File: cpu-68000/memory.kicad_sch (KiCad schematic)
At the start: 0 parts

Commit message: added memory, peripherals
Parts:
- added C? (x6): 100nF, symbol Device:C_Small
- added C? (x4): 4.7µF, symbol Device:C_Small
- added C?: 22µF, symbol Device:C_Polarized_Small
- added U? (x2): IS61C5128AL-10TLI, Package_SO:TSOP-II-44_10.16x18.41mm_P0.8mm, symbol 68komputer-common:IS61C5128AL-10TLI
- added U? (x2): SST39SF040, Package_LCC:PLCC-32_THT-Socket, symbol 68komputer-common:SST39SF040
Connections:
- new net +5V: C?.1, C?.1, C?.1, C?.1, C?.1, C?.1, C?.1, C?.1, C?.1, C?.1, C?.1, U?.11 (VDD), U?.11 (VDD), U?.32 (VCC), U?.32 (VCC), U?.33 (VDD), U?.33 (VDD)
- new net A1: U?.12 (A0), U?.12 (A0), U?.3 (A0), U?.3 (A0)
- new net A10: U?.20 (A9), U?.20 (A9), U?.26 (A9), U?.26 (A9)
- new net A11: U?.23 (A10), U?.23 (A10), U?.26 (A10), U?.26 (A10)
- new net A12: U?.25 (A11), U?.25 (A11), U?.27 (A11), U?.27 (A11)
- new net A13: U?.28 (A12), U?.28 (A12), U?.4 (A12), U?.4 (A12)
- new net A14: U?.28 (A13), U?.28 (A13), U?.29 (A13), U?.29 (A13)
- new net A15: U?.29 (A14), U?.29 (A14), U?.30 (A14), U?.30 (A14)
- new net A16: U?.3 (A15), U?.3 (A15), U?.38 (A15), U?.38 (A15)
- new net A17: U?.2 (A16), U?.2 (A16), U?.39 (A16), U?.39 (A16)
- new net A18: U?.30 (A17), U?.30 (A17), U?.40 (A17), U?.40 (A17)
- new net A19: U?.1 (A18), U?.1 (A18), U?.41 (A18), U?.41 (A18)
- new net A2: U?.11 (A1), U?.11 (A1), U?.4 (A1), U?.4 (A1)
- new net A3: U?.10 (A2), U?.10 (A2), U?.5 (A2), U?.5 (A2)
- new net A4: U?.6 (A3), U?.6 (A3), U?.9 (A3), U?.9 (A3)
- new net A5: U?.7 (A4), U?.7 (A4), U?.8 (A4), U?.8 (A4)
- new net A6: U?.16 (A5), U?.16 (A5), U?.7 (A5), U?.7 (A5)
- new net A7: U?.17 (A6), U?.17 (A6), U?.6 (A6), U?.6 (A6)
- new net A8: U?.18 (A7), U?.18 (A7), U?.5 (A7), U?.5 (A7)
- new net A9: U?.19 (A8), U?.19 (A8), U?.27 (A8), U?.27 (A8)
- new net D0: U?.13 (D0), U?.9 (I/O0)
- new net D1: U?.10 (I/O1), U?.14 (D1)
- new net D10: U?.13 (I/O2), U?.15 (D2)
- new net D11: U?.14 (I/O3), U?.17 (D3)
- new net D12: U?.18 (D4), U?.31 (I/O4)
- new net D13: U?.19 (D5), U?.32 (I/O5)
- new net D14: U?.20 (D6), U?.35 (I/O6)
- new net D15: U?.21 (D7), U?.36 (I/O7)
- new net D2: U?.13 (I/O2), U?.15 (D2)
- new net D3: U?.14 (I/O3), U?.17 (D3)
- new net D4: U?.18 (D4), U?.31 (I/O4)
- new net D5: U?.19 (D5), U?.32 (I/O5)
- new net D6: U?.20 (D6), U?.35 (I/O6)
- new net D7: U?.21 (D7), U?.36 (I/O7)
- new net D8: U?.13 (D0), U?.9 (I/O0)
- new net D9: U?.10 (I/O1), U?.14 (D1)
- new net GND: C?.2, C?.2, C?.2, C?.2, C?.2, C?.2, C?.2, C?.2, C?.2, C?.2, C?.2, U?.12 (GND), U?.12 (GND), U?.16 (GND), U?.16 (GND), U?.34 (GND), U?.34 (GND)
- new net ~{LDS}: U?.15 (~{WE}), U?.24 (~{OE})
- new net ~{LWE}: U?.31 (~{WE}), U?.37 (~{OE})
- new net ~{RAM_CS}: U?.8 (~{CE}), U?.8 (~{CE})
- new net ~{ROM_CS}: U?.22 (~{CS}), U?.22 (~{CS})
- new net ~{UDS}: U?.15 (~{WE}), U?.24 (~{OE})
- new net ~{UWE}: U?.31 (~{WE}), U?.37 (~{OE})
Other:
- note added: "High"
- note added: "Low"

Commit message: Peripherals and general connection stuff
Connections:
- net ~{LDS} is gone; now on net ~{LWE}: U?.15 (~{WE}), U?.24 (~{OE})
- net ~{UDS} is gone; now on net ~{UWE}: U?.15 (~{WE}), U?.24 (~{OE})
- net ~{LWE}: no longer U?.31 (~{WE}), U?.37 (~{OE})
- net ~{UWE}: no longer U?.31 (~{WE}), U?.37 (~{OE})
- new net ~{LOE}: U?.31 (~{WE}), U?.37 (~{OE})
- new net ~{UOE}: U?.31 (~{WE}), U?.37 (~{OE})
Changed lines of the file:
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@@
     (effects (font (size 1.27 1.27)) (justify right))
   )
-  (hierarchical_label "~{LWE}" (shape input) (at 46.99 86.36 180)
+  (hierarchical_label "~{LOE}" (shape input) (at 46.99 86.36 180)
     (effects (font (size 1.27 1.27)) (justify right))
   )
-  (hierarchical_label "~{LDS}" (shape input) (at 46.99 88.9 180)
+  (hierarchical_label "~{LWE}" (shape input) (at 46.99 88.9 180)
     (effects (font (size 1.27 1.27)) (justify right))
   )
@@
     (effects (font (size 1.27 1.27)) (justify right))
   )
-  (hierarchical_label "~{UWE}" (shape input) (at 46.99 178.435 180)
+  (hierarchical_label "~{UOE}" (shape input) (at 46.99 178.435 180)
     (effects (font (size 1.27 1.27)) (justify right))
   )
-  (hierarchical_label "~{UDS}" (shape input) (at 46.99 180.975 180)
+  (hierarchical_label "~{UWE}" (shape input) (at 46.99 180.975 180)
     (effects (font (size 1.27 1.27)) (justify right))
   )
@@
     (effects (font (size 1.27 1.27)) (justify right))
   )
-  (hierarchical_label "~{LWE}" (shape input) (at 118.11 83.82 180)
+  (hierarchical_label "~{LOE}" (shape input) (at 118.11 83.82 180)
     (effects (font (size 1.27 1.27)) (justify right))
   )
-  (hierarchical_label "~{LDS}" (shape input) (at 118.11 86.36 180)
+  (hierarchical_label "~{LWE}" (shape input) (at 118.11 86.36 180)
     (effects (font (size 1.27 1.27)) (justify right))
   )
@@
     (effects (font (size 1.27 1.27)) (justify right))
   )
-  (hierarchical_label "~{UWE}" (shape input) (at 118.11 175.895 180)
+  (hierarchical_label "~{UOE}" (shape input) (at 118.11 175.895 180)
     (effects (font (size 1.27 1.27)) (justify right))
   )
-  (hierarchical_label "~{UDS}" (shape input) (at 118.11 178.435 180)
+  (hierarchical_label "~{UWE}" (shape input) (at 118.11 178.435 180)
     (effects (font (size 1.27 1.27)) (justify right))
   )

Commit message: More backplane stuff; added footprints for most
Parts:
- removed C?: 22µF, symbol Device:C_Polarized_Small
- added C411, C412: 10µF, Capacitor_Tantalum_SMD:CP_EIA-3216-18_Kemet-A, symbol Device:C_Polarized_Small
- C401, C402, C403, C404, C405, C406, C407, C408, C409, C410: renamed from C?; footprint (none) -> Capacitor_SMD:C_0805_2012Metric
- gave numbers to parts that had none: 4
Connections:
- net +5V: now also C411.1, C412.1
- net GND: now also C411.2, C412.2
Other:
- moved on the sheet: C405, C406, C407, C408, C409, C410

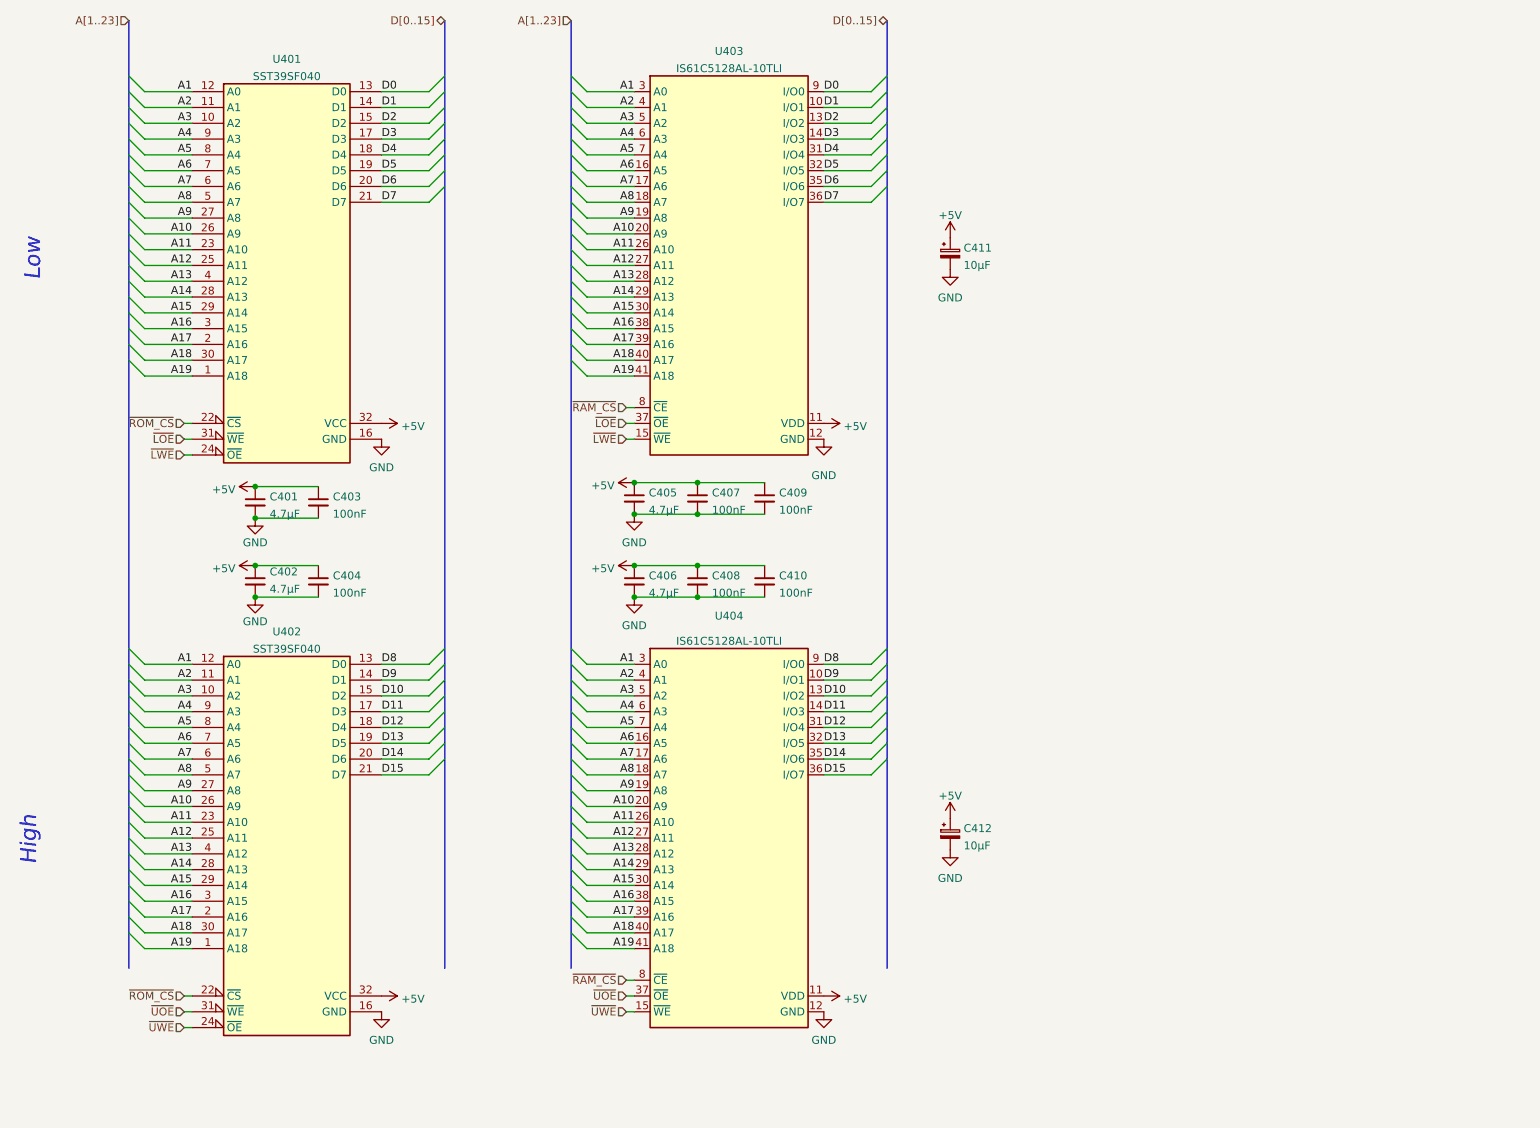
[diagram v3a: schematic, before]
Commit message: start pcb for main cpu
- mostly finish schematic for 68000 cpu; added the missing reset/NMI
  switches

- added footprints for LED indicators

- also added 3d models for fuses, DIN connector, etc
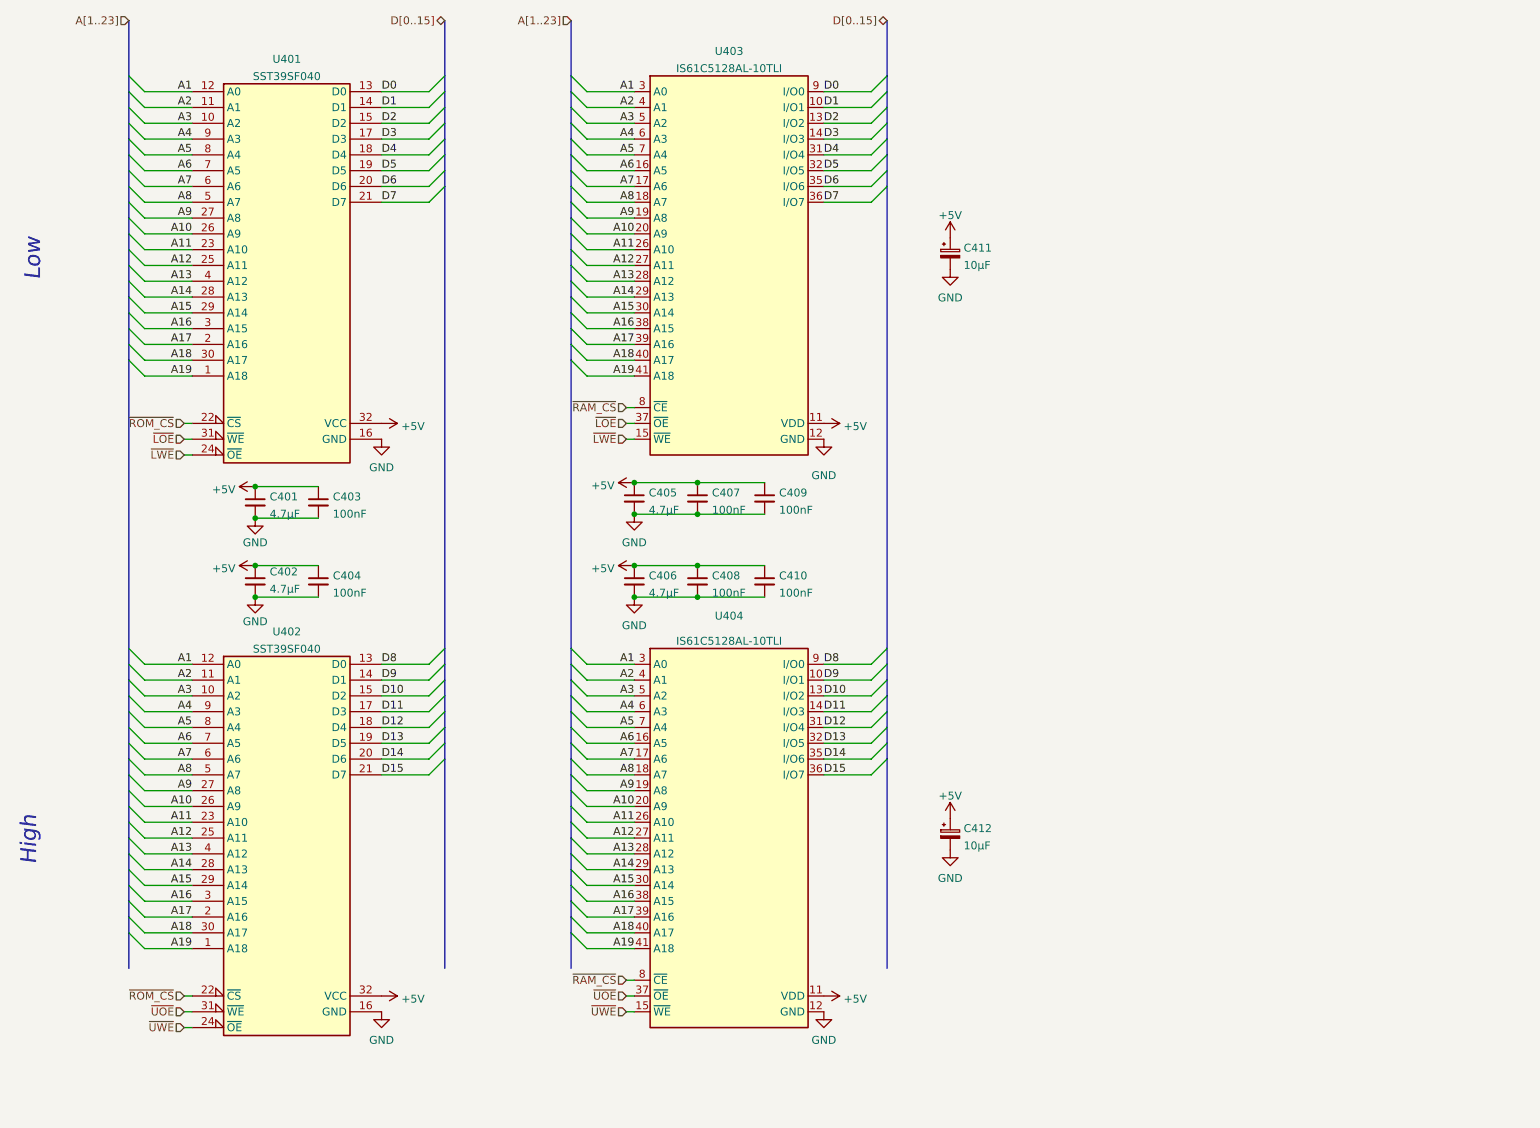
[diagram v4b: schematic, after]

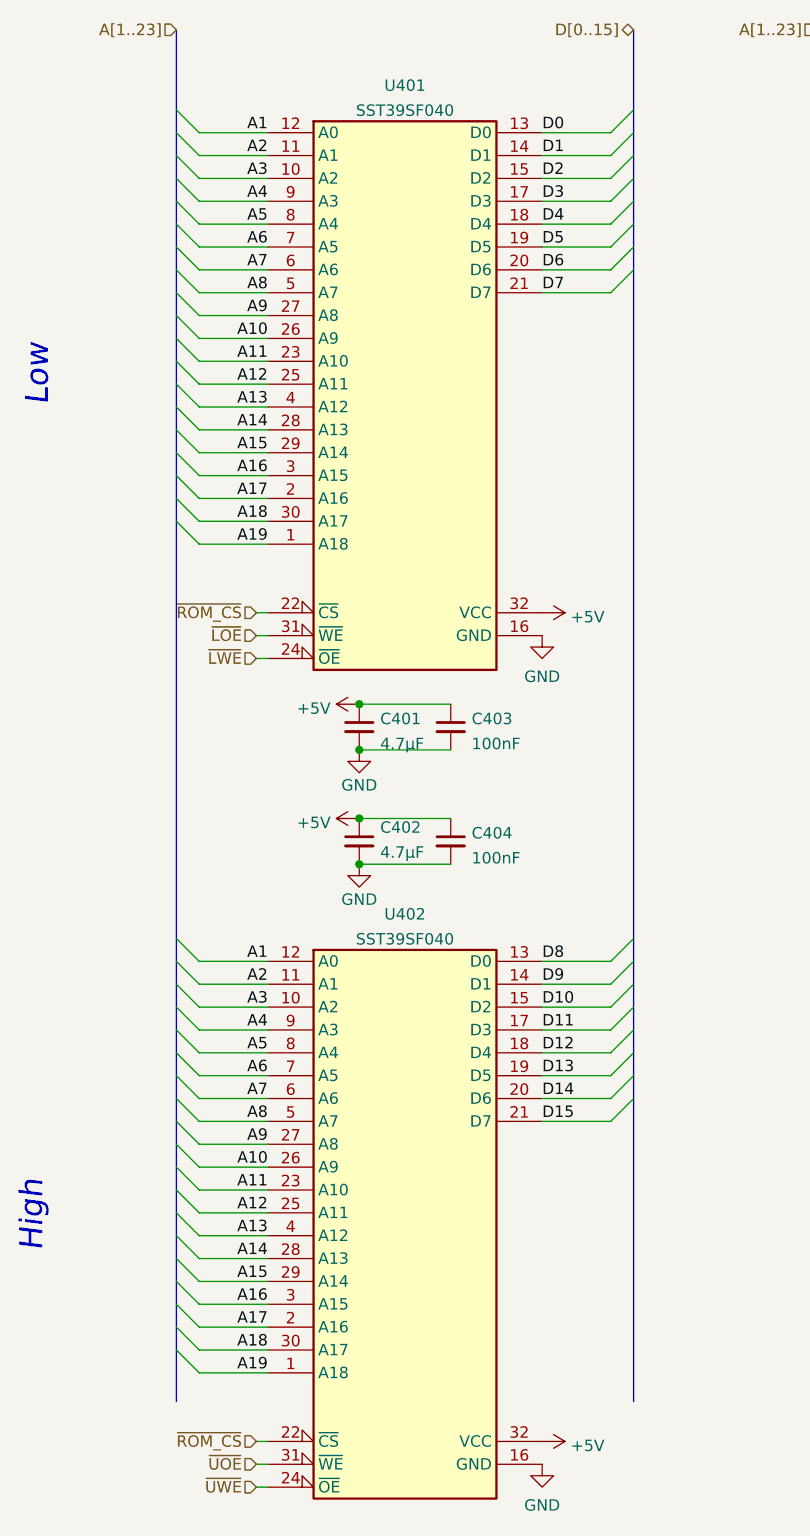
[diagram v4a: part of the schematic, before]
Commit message: Placed most items on pcb
- Laid out most components where they should go on the board; mostly
  routed the connector side of the bus buffers and the address bus

- Added 3d models for PLCC sockets, RTC clock module
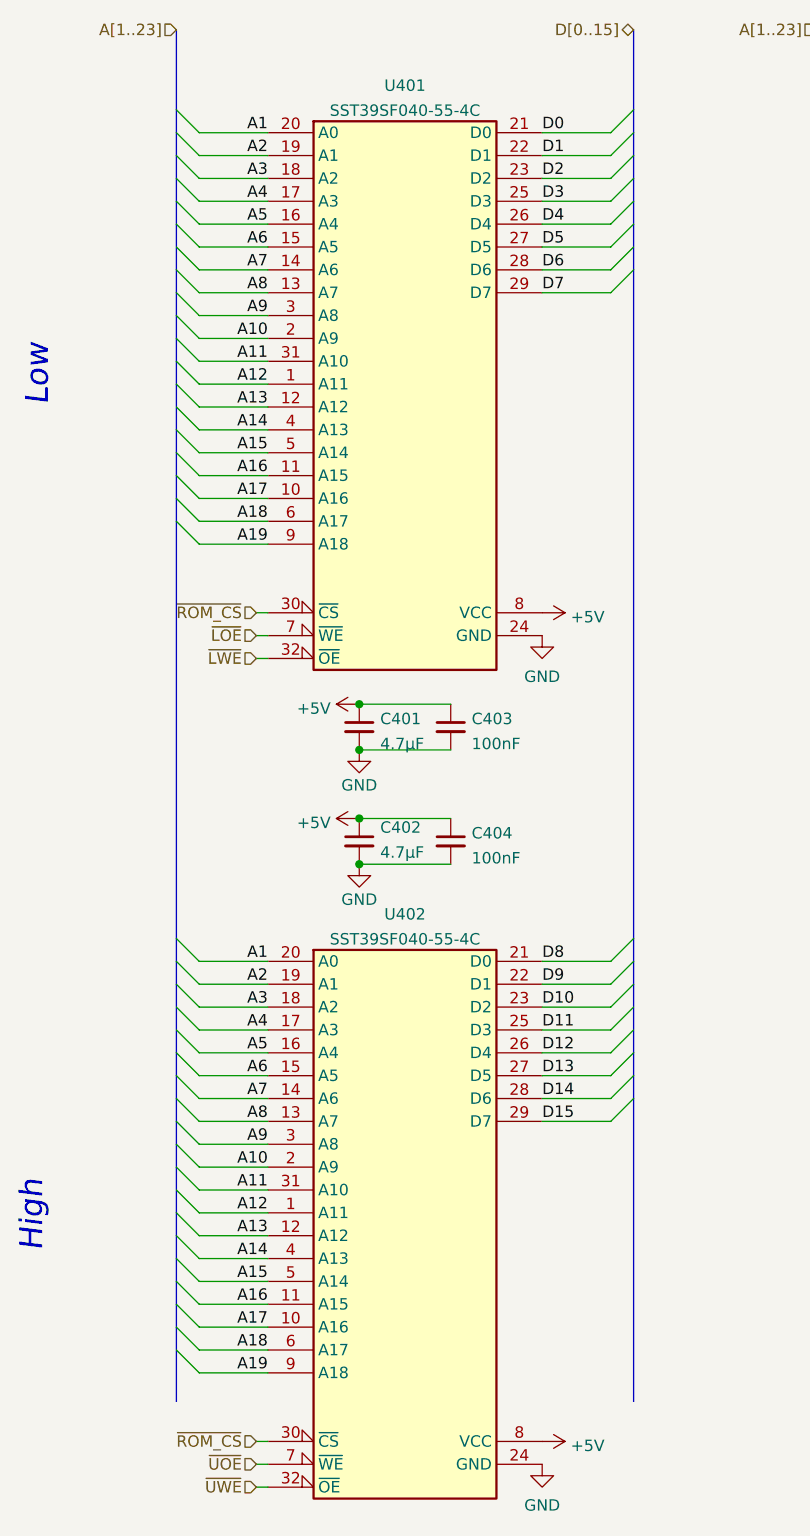
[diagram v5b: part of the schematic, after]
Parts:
- removed U401, U402: SST39SF040, Package_LCC:PLCC-32_THT-Socket, symbol 68komputer-common:SST39SF040
- added U401, U402: SST39SF040-55-4C, Package_SO:TSOP-I-32_11.8x8mm_P0.5mm, symbol 68komputer-common:SST39SF040-XX-4X-W
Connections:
- net +5V: now also U401.8 (VCC), U402.8 (VCC)
- net A1: now also U401.20 (A0), U402.20 (A0)
- net A10: now also U401.2 (A9), U402.2 (A9)
- net A11: now also U401.31 (A10), U402.31 (A10)
- net A12: now also U401.1 (A11), U402.1 (A11)
- net A13: now also U401.12 (A12), U402.12 (A12)
- net A14: now also U401.4 (A13), U402.4 (A13)
- net A15: now also U401.5 (A14), U402.5 (A14)
- net A16: now also U401.11 (A15), U402.11 (A15)
- net A17: now also U401.10 (A16), U402.10 (A16)
- net A18: now also U401.6 (A17), U402.6 (A17)
- net A19: now also U401.9 (A18), U402.9 (A18)
- net A2: now also U401.19 (A1), U402.19 (A1)
- net A3: now also U401.18 (A2), U402.18 (A2)
- net A4: now also U401.17 (A3), U402.17 (A3)
- net A5: now also U401.16 (A4), U402.16 (A4)
- net A6: now also U401.15 (A5), U402.15 (A5)
- net A7: now also U401.14 (A6), U402.14 (A6)
- net A8: now also U401.13 (A7), U402.13 (A7)
- net A9: now also U401.3 (A8), U402.3 (A8)
- net D0: now also U401.21 (D0)
- net D1: now also U401.22 (D1)
- net D10: now also U402.23 (D2)
- net D11: now also U402.25 (D3)
- net D12: now also U402.26 (D4)
- net D13: now also U402.27 (D5)
- net D14: now also U402.28 (D6)
- net D15: now also U402.29 (D7)
- net D2: now also U401.23 (D2)
- net D3: now also U401.25 (D3)
- net D4: now also U401.26 (D4)
- net D5: now also U401.27 (D5)
- net D6: now also U401.28 (D6)
- net D7: now also U401.29 (D7)
- net D8: now also U402.21 (D0)
- net D9: now also U402.22 (D1)
- net GND: now also U401.24 (GND), U402.24 (GND)
- net ~{LOE}: now also U401.7 (~{WE})
- net ~{LWE}: now also U401.32 (~{OE})
- net ~{ROM_CS}: now also U401.30 (~{CS}), U402.30 (~{CS})
- net ~{UOE}: now also U402.7 (~{WE})
- net ~{UWE}: now also U402.32 (~{OE})
